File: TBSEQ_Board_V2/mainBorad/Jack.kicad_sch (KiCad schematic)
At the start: 8 parts

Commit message: mainboard
PWS,Digi
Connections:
- net A+CV_MIX: no longer DgJ11.4 (3)
- net A+GATE: no longer DgJ12.4 (3)
- net A+LineOut: no longer DgJ10.R1
- net A+SyncOut: no longer DgJ13.4 (3)
- net D+5V_SyncIn: now also DgJ9.2 (2_1), DgJ9.3 (2_2); no longer DgJ9.4 (3)
- net D+PlugIn_SyncIn: now also DgJ9.4 (3); no longer DgJ9.3 (2_2)
- net GNDA: no longer DgJ10.SS1
- no-connect marks 3 -> 7

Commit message: mainBoard
AnInterface
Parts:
- removed DgJ10: MJ-462, MJ462, symbol SamacSys_Parts:MJ-462
- removed DgJ14, DgJ15: Conn_01x03, Connector_PinHeader_2.54mm:PinHeader_1x03_P2.54mm_Vertical, symbol Connector_Generic:Conn_01x03
- added AnPw1: AnPw, Connector_PinSocket_2.54mm:PinSocket_1x03_P2.54mm_Vertical, symbol Connector_Generic:Conn_01x03
- added DgPw1: DgPw, Connector_PinSocket_2.54mm:PinSocket_1x03_P2.54mm_Vertical, symbol Connector_Generic:Conn_01x03
- added PanelJ1: Conn_02x20_Odd_Even, Connector_PinSocket_2.54mm:PinSocket_2x20_P2.54mm_Vertical, symbol Connector_Generic:Conn_02x20_Odd_Even
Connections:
- net A+CV_MIX: now also DgJ16.2 (Pin_2); no longer DgJ16.5 (Pin_5)
- net A+GATE: now also DgJ16.5 (Pin_5); no longer DgJ16.4 (Pin_4)
- net A+SLIDE: now also DgJ16.3 (Pin_3); no longer DgJ16.2 (Pin_2)
- net A+TEMPO: now also PanelJ1.1 (Pin_1)
- net A-ACC: now also DgJ16.4 (Pin_4); no longer DgJ16.3 (Pin_3)
- net D+3.3V: now also DgPw1.2 (Pin_2), PanelJ1.2 (Pin_2)
- net GNDA: now also AnPw1.3 (Pin_3), PanelJ1.16 (Pin_16), PanelJ1.29 (Pin_29), PanelJ1.31 (Pin_31), PanelJ1.33 (Pin_33), PanelJ1.36 (Pin_36)
- net GNDD: now also DgPw1.3 (Pin_3), PanelJ1.7 (Pin_7), PanelJ1.8 (Pin_8)
- new net A+12V: AnPw1.1 (Pin_1), PanelJ1.12 (Pin_12)
- new net A+5.333V: AnPw1.2 (Pin_2), PanelJ1.14 (Pin_14)
- new net A_VR2_CCW: PanelJ1.17 (Pin_17)
- new net A_VR2_CW: PanelJ1.21 (Pin_21)
- new net A_VR2_WIPER: PanelJ1.19 (Pin_19)
- new net A_VR3_CCW: PanelJ1.18 (Pin_18)
- new net A_VR3_CW: PanelJ1.22 (Pin_22)
- new net A_VR3_WIPER: PanelJ1.20 (Pin_20)
- new net A_VR4_1_CCW: PanelJ1.23 (Pin_23)
- new net A_VR4_1_CW: PanelJ1.27 (Pin_27)
- new net A_VR4_1_WIPER: PanelJ1.25 (Pin_25)
- new net A_VR4_2_CCW: PanelJ1.24 (Pin_24)
- new net A_VR4_2_CW: PanelJ1.28 (Pin_28)
- new net A_VR4_2_WIPER: PanelJ1.26 (Pin_26)
- new net A_VR5_CCW: PanelJ1.30 (Pin_30)
- new net A_VR5_CW: PanelJ1.34 (Pin_34)
- new net A_VR5_WIPER: PanelJ1.32 (Pin_32)
- new net A_VR6_CCW: PanelJ1.35 (Pin_35)
- new net A_VR6_WIPER_CW: PanelJ1.37 (Pin_37), PanelJ1.39 (Pin_39)
- new net A_VR7_CW: PanelJ1.40 (Pin_40)
- new net A_VR7_WIPER: PanelJ1.38 (Pin_38)
- new net A_VR8_CCW: PanelJ1.11 (Pin_11)
- new net A_VR8_CW: PanelJ1.15 (Pin_15)
- new net A_VR8_WIPER: PanelJ1.13 (Pin_13)
- new net D+5V: DgPw1.1 (Pin_1), PanelJ1.5 (Pin_5)
- new net D_I2C_SCL: PanelJ1.6 (Pin_6)
- new net D_I2C_SDA: PanelJ1.4 (Pin_4)
- no-connect marks 7 -> 6
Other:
- note added: "A_VR6_WIPERはCWと接続"
- note added: "A_VR7_CCWはGNDAと接続"
- note added: "Power"
- note removed: "AUDIO OUT"
- note removed: "TEMPO"
- moved on the sheet: DgJ16

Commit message: mainBoard
VCO
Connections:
- net A_VR2_CCW is gone; now on net GNDA: PanelJ1.17 (Pin_17)
- net A_VR2_CW is gone; now on net A+5.333V: PanelJ1.21 (Pin_21)
- net GNDA: no longer PanelJ1.29 (Pin_29), PanelJ1.31 (Pin_31), PanelJ1.33 (Pin_33)
- new net A+VCO_SAW: PanelJ1.31 (Pin_31)
- new net A+VCO_SQU: PanelJ1.29 (Pin_29)
- new net A+VCO_WAVE: PanelJ1.33 (Pin_33)
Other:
- note added: "A_VR2_CCWはGNDAと接続"
- note added: "A_VR2_CWはA+5.333Vと接続"
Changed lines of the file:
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@@
 	(paper "A4")
-	(junction
-		(at 184.15 80.01)
-		(diameter 0)
-		(color 0 0 0 0)
-	)
 	(junction
 		(at 124.46 91.44)
@@
 	)
 	(junction
-		(at 184.15 77.47)
-		(diameter 0)
-		(color 0 0 0 0)
-	)
-	(junction
 		(at 123.19 31.75)
 		(diameter 0)
@@
 	(wire
 		(pts
+			(xy 213.36 77.47) (xy 215.9 77.47)
+		)
+		(stroke
+			(width 0)
+			(type default)
+		)
+	)
+	(wire
+		(pts
 			(xy 212.09 85.09) (xy 215.9 85.09)
 		)
@@
 	(wire
 		(pts
-			(xy 184.15 80.01) (xy 215.9 80.01)
-		)
-		(stroke
-			(width 0)
-			(type default)
-		)
-	)
-	(wire
-		(pts
-			(xy 215.9 74.93) (xy 184.15 74.93)
-		)
-		(stroke
-			(width 0)
-			(type default)
-		)
-	)
-	(wire
-		(pts
 			(xy 231.14 54.61) (xy 228.6 54.61)
 		)
@@
 	(wire
 		(pts
-			(xy 213.36 59.69) (xy 215.9 59.69)
-		)
-		(stroke
-			(width 0)
-			(type default)
-		)
-	)
-	(wire
-		(pts
 			(xy 135.89 146.05) (xy 129.54 146.05)
 		)
@@
 	(wire
 		(pts
+			(xy 213.36 80.01) (xy 215.9 80.01)
+		)
+		(stroke
+			(width 0)
+			(type default)
+		)
+	)
+	(wire
+		(pts
 			(xy 228.6 69.85) (xy 231.14 69.85)
 		)
@@
 	(wire
 		(pts
-			(xy 184.15 74.93) (xy 184.15 77.47)
-		)
-		(stroke
-			(width 0)
-			(type default)
-		)
-	)
-	(wire
-		(pts
 			(xy 120.65 34.29) (xy 123.19 34.29)
 		)
@@
 	(wire
 		(pts
+			(xy 179.07 59.69) (xy 179.07 91.44)
+		)
+		(stroke
+			(width 0)
+			(type default)
+		)
+	)
+	(wire
+		(pts
 			(xy 120.65 66.04) (xy 124.46 66.04)
 		)
@@
 	(wire
 		(pts
-			(xy 184.15 80.01) (xy 184.15 86.36)
-		)
-		(stroke
-			(width 0)
-			(type default)
-		)
-	)
-	(wire
-		(pts
 			(xy 228.6 74.93) (xy 231.14 74.93)
 		)
@@
 	(wire
 		(pts
-			(xy 184.15 77.47) (xy 215.9 77.47)
-		)
-		(stroke
-			(width 0)
-			(type default)
-		)
-	)
-	(wire
-		(pts
 			(xy 228.6 85.09) (xy 231.14 85.09)
 		)
@@
 	(wire
 		(pts
+			(xy 213.36 74.93) (xy 215.9 74.93)
+		)
+		(stroke
+			(width 0)
+			(type default)
+		)
+	)
+	(wire
+		(pts
 			(xy 228.6 64.77) (xy 231.14 64.77)
 		)
@@
 	(wire
 		(pts
+			(xy 179.07 59.69) (xy 215.9 59.69)
+		)
+		(stroke
+			(width 0)
+			(type default)
+		)
+	)
+	(wire
+		(pts
 			(xy 213.36 57.15) (xy 215.9 57.15)
-		)
-		(stroke
-			(width 0)
-			(type default)
-		)
-	)
-	(wire
-		(pts
-			(xy 184.15 77.47) (xy 184.15 80.01)
 		)
 		(stroke
@@
 		)
 	)
+	(text "A_VR2_CCWはGNDAと接続"
+		(exclude_from_sim no)
+		(at 191.008 60.452 0)
+		(effects
+			(font
+				(size 1.27 1.27)
+			)
+		)
+	)
 	(text "SYNC IN"
 		(exclude_from_sim no)
@@
 		)
 	)
+	(text "A_VR2_CWはA+5.333Vと接続"
+		(exclude_from_sim no)
+		(at 189.23 65.278 0)
+		(effects
+			(font
+				(size 1.27 1.27)
+			)
+		)
+	)
 	(text "A_VR6_WIPERはCWと接続"
 		(exclude_from_sim no)
@@
 		)
 	)
+	(global_label "A+VCO_WAVE"
+		(shape output)
+		(at 213.36 80.01 180)
+		(fields_autoplaced yes)
+		(effects
+			(font
+				(size 1.27 1.27)
+			)
+			(justify right)
+		)
+		(property "Intersheetrefs" "${INTERSHEET_REFS}"
+			(at 198.2795 80.01 0)
+			(effects
+				(font
+					(size 1.27 1.27)
+				)
+				(justify right)
+				(hide yes)
+			)
+		)
+	)
 	(global_label "D_I2C_SCL"
 		(shape output)
@@
 		)
 	)
-	(global_label "A_VR2_CCW"
-		(shape output)
-		(at 213.36 59.69 180)
-		(fields_autoplaced yes)
-		(effects
-			(font
-				(size 1.27 1.27)
-			)
-			(justify right)
-		)
-		(property "Intersheetrefs" "${INTERSHEET_REFS}"
-			(at 199.7915 59.69 0)
+	(global_label "A+VCO_SAW"
+		(shape output)
+		(at 213.36 77.47 180)
+		(fields_autoplaced yes)
+		(effects
+			(font
+				(size 1.27 1.27)
+			)
+			(justify right)
+		)
+		(property "Intersheetrefs" "${INTERSHEET_REFS}"
+			(at 199.3076 77.47 0)
 			(effects
 				(font
@@
 		)
 	)
+	(global_label "A+5.333V"
+		(shape input)
+		(at 213.36 64.77 180)
+		(fields_autoplaced yes)
+		(effects
+			(font
+				(size 1.27 1.27)
+			)
+			(justify right)
+		)
+		(property "Intersheetrefs" "${INTERSHEET_REFS}"
+			(at 201.1824 64.77 0)
+			(effects
+				(font
+					(size 1.27 1.27)
+				)
+				(justify right)
+				(hide yes)
+			)
+		)
+	)
 	(global_label "A+12V"
 		(shape output)
@@
 		(property "Intersheetrefs" "${INTERSHEET_REFS}"
 			(at 205.2343 44.45 0)
-			(effects
-				(font
-					(size 1.27 1.27)
-				)
-				(justify right)
-				(hide yes)
-			)
-		)
-	)
-	(global_label "A_VR2_CW"
-		(shape output)
-		(at 213.36 64.77 180)
-		(fields_autoplaced yes)
-		(effects
-			(font
-				(size 1.27 1.27)
-			)
-			(justify right)
-		)
-		(property "Intersheetrefs" "${INTERSHEET_REFS}"
-			(at 201.0615 64.77 0)
 			(effects
 				(font
@@
 		(property "Intersheetrefs" "${INTERSHEET_REFS}"
 			(at 96.1352 140.97 0)
+			(effects
+				(font
+					(size 1.27 1.27)
+				)
+				(justify right)
+				(hide yes)
+			)
+		)
+	)
+	(global_label "A+VCO_SQU"
+		(shape output)
+		(at 213.36 74.93 180)
+		(fields_autoplaced yes)
+		(effects
+			(font
+				(size 1.27 1.27)
+			)
+			(justify right)
+		)
+		(property "Intersheetrefs" "${INTERSHEET_REFS}"
+			(at 199.1866 74.93 0)
 			(effects
 				(font
@@
 	)
 	(symbol
-		(lib_id "power:GNDA")
-		(at 184.15 86.36 0)
-		(unit 1)
-		(exclude_from_sim no)
-		(in_bom yes)
-		(on_board yes)
-		(dnp no)
-		(fields_autoplaced yes)
-		(property "Reference" "#PWR025"
-			(at 184.15 92.71 0)
-			(effects
-				(font
-					(size 1.27 1.27)
-				)
-				(hide yes)
-			)
-		)
-		(property "Value" "GNDA"
-			(at 184.15 91.44 0)
-			(effects
-				(font
-					(size 1.27 1.27)
-				)
-			)
-		)
-		(property "Footprint" ""
-			(at 184.15 86.36 0)
-			(effects
-				(font
-					(size 1.27 1.27)
-				)
-				(hide yes)
-			)
-		)
-		(property "Datasheet" ""
-			(at 184.15 86.36 0)
-			(effects
-				(font
-					(size 1.27 1.27)
-				)
-				(hide yes)
-			)
-		)
-		(property "Description" "Power symbol creates a global label with name \"GNDA\" , analog ground"
-			(at 184.15 86.36 0)
-			(effects
-				(font
-					(size 1.27 1.27)
-				)
-				(hide yes)
-			)
-		)
-		(pin "1"
-		)
-		(instances
-			(project "mainBorad"
-				(path "/74b57c73-2ea6-4d1a-baa5-ad46186fbb51/0ae150e0-c08a-4733-b66b-e4b7868d24b7"
-					(reference "#PWR025")
-					(unit 1)
-				)
-			)
-		)
-	)
-	(symbol
 		(lib_id "Connector_Generic:Conn_01x03")
 		(at 140.97 143.51 0)
@@
 					(unit 1)
 				)
+			)
+		)
+	)
+	(symbol
+		(lib_id "power:GNDA")
+		(at 179.07 91.44 0)
+		(unit 1)
+		(exclude_from_sim no)
+		(in_bom yes)
+		(on_board yes)
+		(dnp no)
+		(fields_autoplaced yes)
+		(property "Reference" "#PWR025"
+			(at 179.07 97.79 0)
+			(effects
+				(font
+					(size 1.27 1.27)
+				)
+				(hide yes)
+			)
+		)
+		(property "Value" "GNDA"
+			(at 179.07 96.52 0)
+			(effects
+				(font
+					(size 1.27 1.27)
+				)
+			)
+		)
+		(property "Footprint" ""
+			(at 179.07 91.44 0)
+			(effects
+				(font
+					(size 1.27 1.27)
+				)
+				(hide yes)
+			)
+		)
+		(property "Datasheet" ""
+			(at 179.07 91.44 0)
+			(effects
+				(font
+					(size 1.27 1.27)
+				)
+				(hide yes)
+			)
+		)
+		(property "Description" "Power symbol creates a global label with name \"GNDA\" , analog ground"
+			(at 179.07 91.44 0)
+			(effects
+				(font
+					(size 1.27 1.27)
+				)
+				(hide yes)
+			)
+		)
+		(pin "1"
+		)
+		(instances
+			(project "mainBorad"
+				(path "/74b57c73-2ea6-4d1a-baa5-ad46186fbb51/0ae150e0-c08a-4733-b66b-e4b7868d24b7"
+					(reference "#PWR025")
+					(unit 1)
+				)

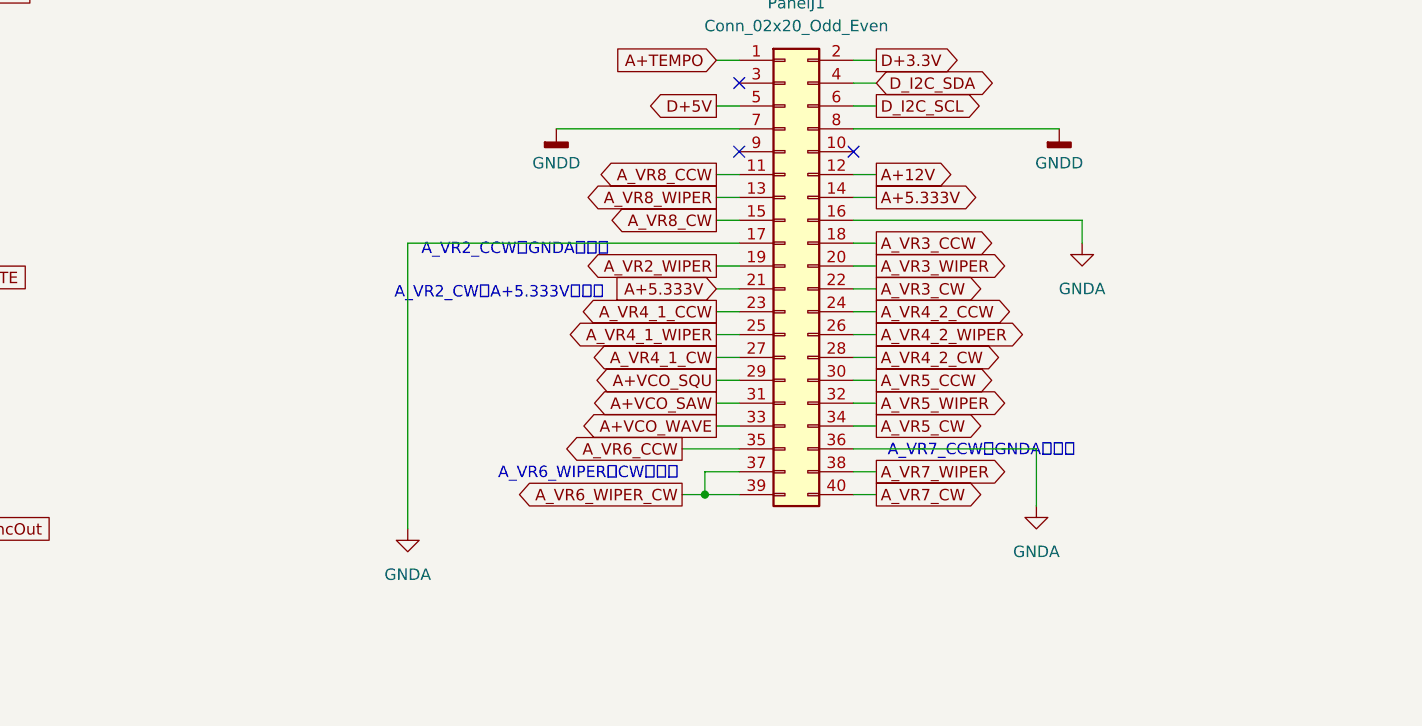
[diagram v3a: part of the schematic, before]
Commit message: mainboard
部品を全部配置しただけ
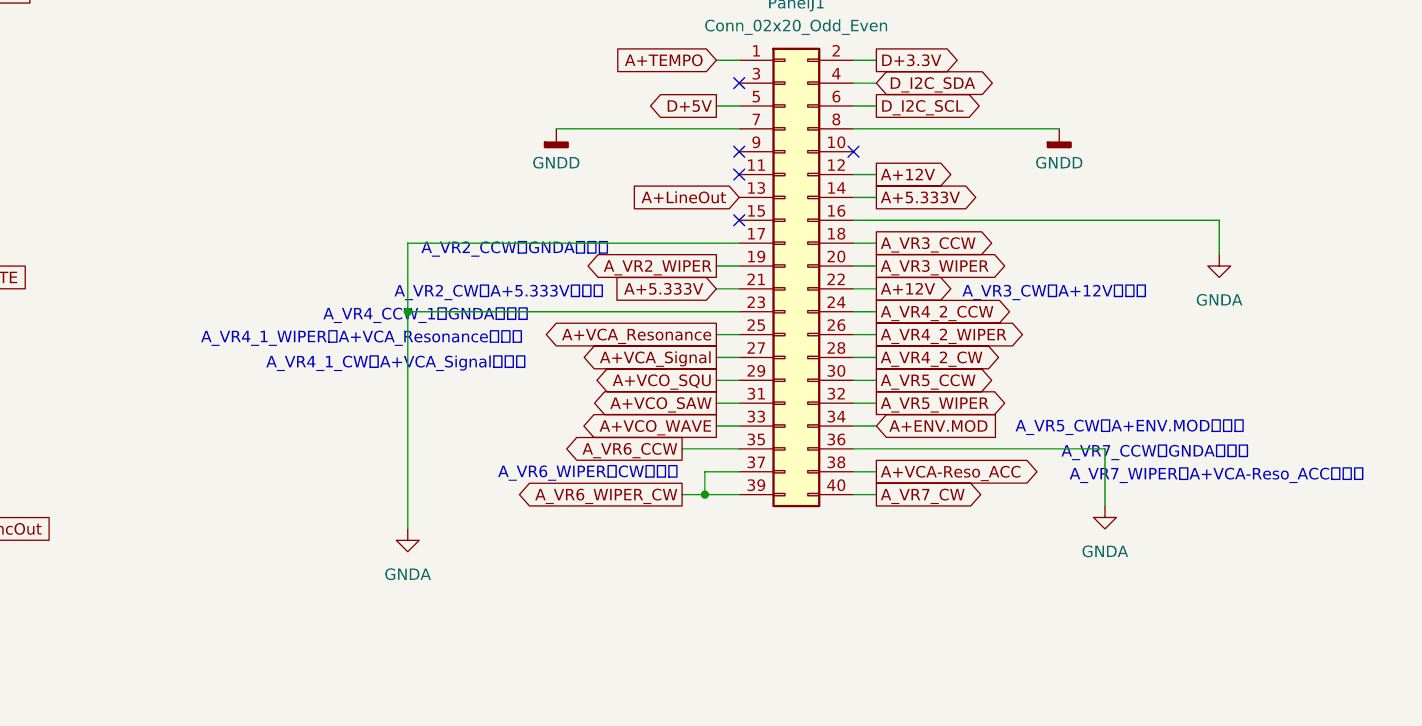
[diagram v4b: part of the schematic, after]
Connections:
- net A_VR3_CW is gone; now on net A+12V: PanelJ1.22 (Pin_22)
- net A_VR4_1_CCW is gone; now on net GNDA: PanelJ1.23 (Pin_23)
- net A_VR4_1_CW renamed A+VCA_Signal
- net A_VR4_1_WIPER renamed A+VCA_Resonance
- net A_VR5_CW renamed A+ENV.MOD
- net A_VR7_WIPER renamed A+VCA-Reso_ACC
- net A_VR8_CCW: no longer names the net of PanelJ1.11 (Pin_11)
- net A_VR8_CW: no longer names the net of PanelJ1.15 (Pin_15)
- net A_VR8_WIPER renamed A+LineOut
- no-connect marks 6 -> 8
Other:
- note added: "A_VR3_CWはA+12Vと接続"
- note added: "A_VR4_1_CWはA+VCA_Signalと接続"
- note added: "A_VR4_1_WIPERはA+VCA_Resonanceと接続"
- note added: "A_VR4_CCW_1はGNDAと接続"
- note added: "A_VR5_CWはA+ENV.MODと接続"
- note added: "A_VR7_WIPERはA+VCA-Reso_ACCと接続"

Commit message: mainBoradV2.5
修正中
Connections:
- net A+SyncOut: no longer DgJ13.3 (2_2)
- net D+5V_SyncIn: no longer DgJ9.3 (2_2)
- new net A+SyncOut_Run/Stop: DgJ13.3 (2_2)
- new net D+5V_SyncIn_Run/Stop: DgJ9.3 (2_2)
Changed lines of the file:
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@@
 	(paper "A4")
-	(junction
-		(at 124.46 91.44)
-		(diameter 0)
-		(color 0 0 0 0)
-	)
-	(junction
-		(at 124.46 115.57)
-		(diameter 0)
-		(color 0 0 0 0)
-	)
 	(junction
 		(at 123.19 31.75)
@@
 	(wire
 		(pts
+			(xy 128.27 118.11) (xy 119.38 118.11)
+		)
+		(stroke
+			(width 0)
+			(type default)
+		)
+	)
+	(wire
+		(pts
 			(xy 179.07 67.31) (xy 215.9 67.31)
 		)
@@
 	(wire
 		(pts
-			(xy 124.46 93.98) (xy 124.46 91.44)
-		)
-		(stroke
-			(width 0)
-			(type default)
-		)
-	)
-	(wire
-		(pts
 			(xy 92.71 118.11) (xy 96.52 118.11)
 		)
@@
 	(wire
 		(pts
-			(xy 124.46 118.11) (xy 124.46 115.57)
-		)
-		(stroke
-			(width 0)
-			(type default)
-		)
-	)
-	(wire
-		(pts
 			(xy 195.58 46.99) (xy 215.9 46.99)
 		)
@@
 	(wire
 		(pts
-			(xy 124.46 91.44) (xy 127 91.44)
+			(xy 120.65 91.44) (xy 127 91.44)
 		)
 		(stroke
@@
 	(wire
 		(pts
-			(xy 119.38 118.11) (xy 124.46 118.11)
-		)
-		(stroke
-			(width 0)
-			(type default)
-		)
-	)
-	(wire
-		(pts
 			(xy 213.36 80.01) (xy 215.9 80.01)
 		)
@@
 	(wire
 		(pts
-			(xy 124.46 115.57) (xy 128.27 115.57)
+			(xy 119.38 115.57) (xy 128.27 115.57)
 		)
 		(stroke
@@
 	(wire
 		(pts
-			(xy 120.65 93.98) (xy 124.46 93.98)
+			(xy 120.65 93.98) (xy 127 93.98)
 		)
 		(stroke
@@
 	(wire
 		(pts
-			(xy 120.65 91.44) (xy 124.46 91.44)
-		)
-		(stroke
-			(width 0)
-			(type default)
-		)
-	)
-	(wire
-		(pts
 			(xy 231.14 52.07) (xy 228.6 52.07)
 		)
@@
 		(pts
 			(xy 179.07 59.69) (xy 215.9 59.69)
-		)
-		(stroke
-			(width 0)
-			(type default)
-		)
-	)
-	(wire
-		(pts
-			(xy 119.38 115.57) (xy 124.46 115.57)
 		)
 		(stroke
@@
 		)
 	)
+	(global_label "D+5V_SyncIn_Run/Stop"
+		(shape input)
+		(at 128.27 118.11 0)
+		(fields_autoplaced yes)
+		(effects
+			(font
+				(size 1.27 1.27)
+			)
+			(justify left)
+		)
+		(property "Intersheetrefs" "${INTERSHEET_REFS}"
+			(at 150.3654 118.11 0)
+			(effects
+				(font
+					(size 1.27 1.27)
+				)
+				(justify left)
+				(hide yes)
+			)
+		)
+	)
 	(global_label "A_VR4_2_CCW"
 		(shape output)
@@
 		(property "Intersheetrefs" "${INTERSHEET_REFS}"
 			(at 244.7085 74.93 0)
+			(effects
+				(font
+					(size 1.27 1.27)
+				)
+				(justify left)
+				(hide yes)
+			)
+		)
+	)
+	(global_label "A+SyncOut_Run{slash}Stop"
+		(shape output)
+		(at 127 93.98 0)
+		(fields_autoplaced yes)
+		(effects
+			(font
+				(size 1.27 1.27)
+			)
+			(justify left)
+		)
+		(property "Intersheetrefs" "${INTERSHEET_REFS}"
+			(at 150.3654 93.98 0)
 			(effects
 				(font
@@
 	)
 	(global_label "D+5V_SyncIn"
-		(shape output)
+		(shape input)
 		(at 128.27 115.57 0)
 		(fields_autoplaced yes)
@@
 	)
 	(global_label "A+SyncOut"
-		(shape input)
+		(shape output)
 		(at 127 91.44 0)
 		(fields_autoplaced yes)
